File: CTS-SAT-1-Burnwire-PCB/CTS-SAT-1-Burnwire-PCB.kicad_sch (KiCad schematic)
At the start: 8 parts, among them J1 Conn_01x04_MountingPin, J2 Conn_01x06_MountingPin, Q1 IPD90N04S4L

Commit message: Layout and routing
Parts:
- added C1: 10u, Capacitor_SMD:C_1206_3216Metric_Pad1.33x1.80mm_HandSolder, symbol Device:C
- added C2: 100n, Capacitor_SMD:C_1206_3216Metric_Pad1.33x1.80mm_HandSolder, symbol Device:C
- added D2: LED, LED_SMD:LED_0603_1608Metric_Pad1.05x0.95mm_HandSolder, symbol Device:LED
- added H1, H3: MountingHole_Pad, MountingHole:MountingHole_2.2mm_M2_Pad, symbol Mechanical:MountingHole_Pad
- added H2, H4: MountingHole_Pad, MountingHole:MountingHole_2.7mm_M2.5_Pad, symbol Mechanical:MountingHole_Pad
- added R4, R5, R6, R7: 0, Resistor_SMD:R_0603_1608Metric_Pad0.98x0.95mm_HandSolder, symbol Device:R
- added R8: 5k1, Resistor_SMD:R_0603_1608Metric_Pad0.98x0.95mm_HandSolder, symbol Device:R
- added R9: 100k, Resistor_SMD:R_0603_1608Metric_Pad0.98x0.95mm_HandSolder, symbol Device:R
- J1: footprint (none) -> Connector_Molex:Molex_PicoBlade_53261-0471_1x04-1MP_P1.25mm_Horizontal
- J2: footprint (none) -> Connector_Molex:Molex_PicoBlade_53261-0671_1x06-1MP_P1.25mm_Horizontal
- R1: footprint (none) -> 00-footprint-lib:AxialBurnResistor
- R2, R3: footprint (none) -> Resistor_SMD:R_0603_1608Metric_Pad0.98x0.95mm_HandSolder
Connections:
- net BURN_CTRL: now also J1.3 (Pin_3)
- net GND: now also J1.1 (Pin_1), J1.2 (Pin_2), C1.2, C2.2, R4.2, R5.2, R6.2, R7.2, R8.2, R9.2
- net VDC: now also C1.1, C2.1
- net at D1.2 (A2), Q1.1 (G), R2.1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: now also D2.2 (A)
- net at J1.4 (Pin_4): now also R9.1
- new net: H1.1, R4.1
- new net: D2.1 (K), R8.1
- new net: H3.1, R6.1
- new net: H2.1, R5.1
- new net: H4.1, R7.1

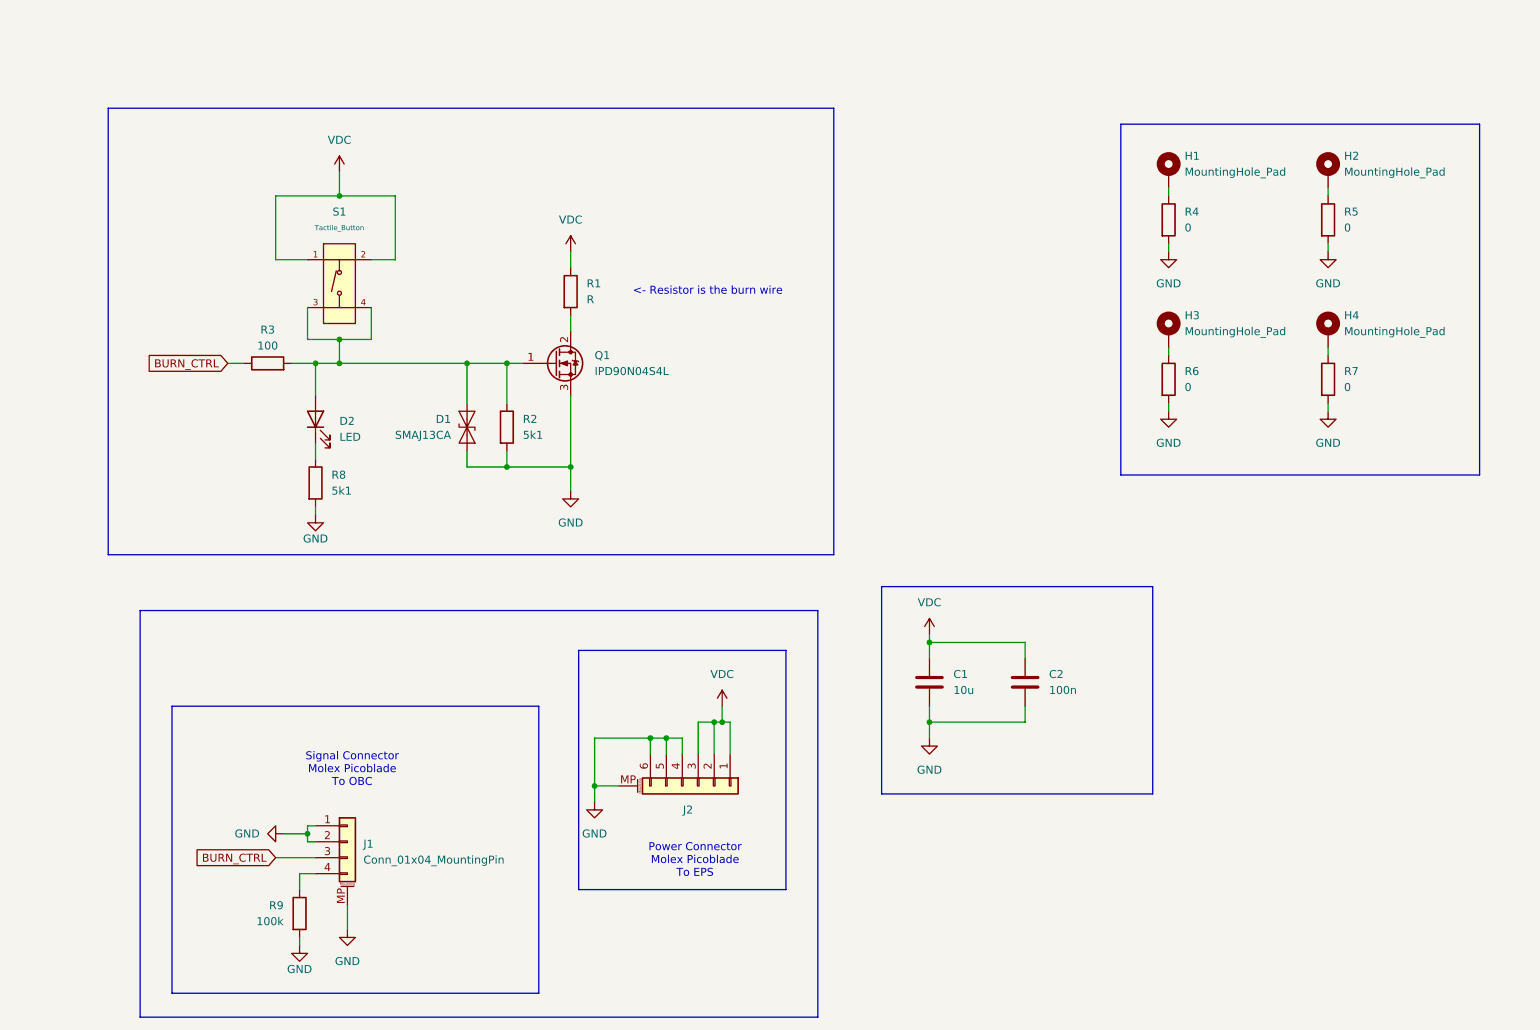
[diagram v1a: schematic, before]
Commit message: Convert to 2-resistor design
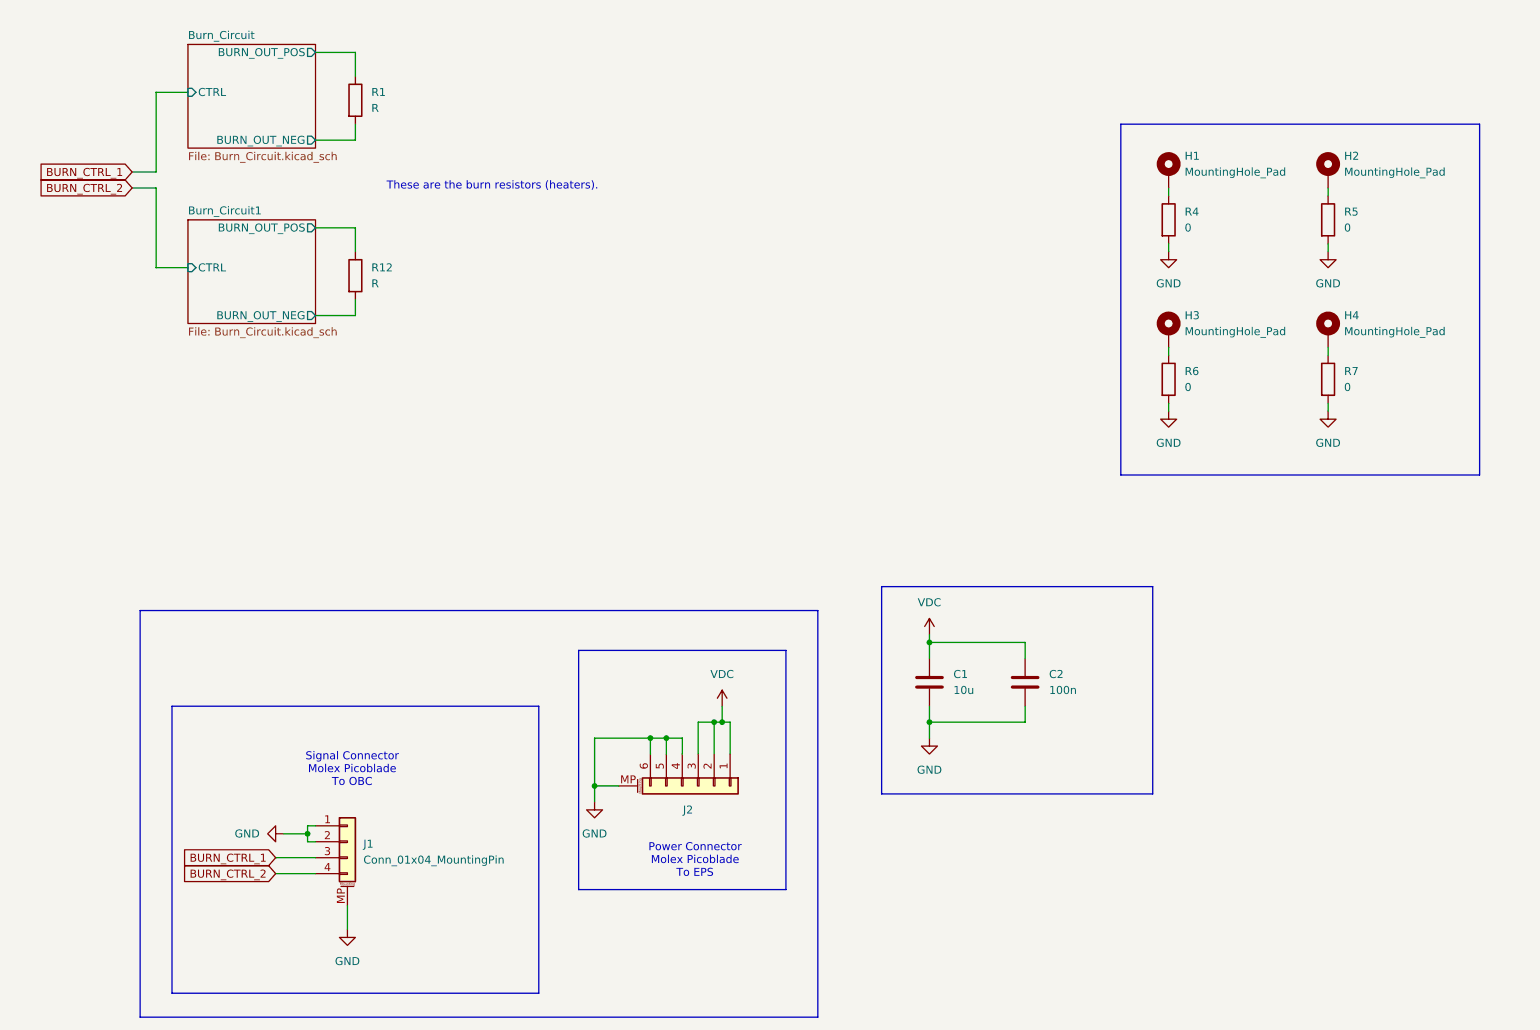
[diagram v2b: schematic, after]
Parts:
- removed D1: SMAJ13CA, Diode_SMD:D_SMA, symbol Diode:SMAJ13CA
- removed D2: LED, LED_SMD:LED_0603_1608Metric_Pad1.05x0.95mm_HandSolder, symbol Device:LED
- removed Q1: IPD90N04S4L, Package_TO_SOT_SMD:TO-252-3_TabPin2, symbol 00-symbol-lib:IPD90N04S4L
- removed R2, R8: 5k1, Resistor_SMD:R_0603_1608Metric_Pad0.98x0.95mm_HandSolder, symbol Device:R
- removed R3: 100, Resistor_SMD:R_0603_1608Metric_Pad0.98x0.95mm_HandSolder, symbol Device:R
- removed R9: 100k, Resistor_SMD:R_0603_1608Metric_Pad0.98x0.95mm_HandSolder, symbol Device:R
- removed S1: Tactile_Button, 00-footprint-lib:SW-SMD_4P-L5.1-W5.1-P3.70-LS6.5-TL-2, symbol 00-symbol-lib:Tactile_Button
- added R12: R, 00-footprint-lib:AxialBurnResistor_No_Cutout, symbol Device:R
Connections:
- net VDC: no longer R1.1
- net Burn_Circuit/BURN_OUT_NEG: now reaches R1.2
- net BURN_CTRL_2: now reaches J1.4 (Pin_4)
- net BURN_CTRL renamed BURN_CTRL_1
- new net Burn_Circuit/BURN_OUT_POS: R1.1
- new net Burn_Circuit1/BURN_OUT_NEG: R12.2
- new net Burn_Circuit1/BURN_OUT_POS: R12.1
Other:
- added sheet Burn_Circuit (Burn_Circuit.kicad_sch)
- added sheet Burn_Circuit1 (Burn_Circuit.kicad_sch)
- note added: "These are the burn resistors (heaters)."
- note removed: "<- Resistor is the burn wire"

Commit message: Update mounting hole diameters
M2 by the resistors and M2.5 by the connectors
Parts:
- H1, H3: footprint MountingHole:MountingHole_2.2mm_M2_Pad -> MountingHole:MountingHole_2.7mm_M2.5_Pad
- H2, H4: footprint MountingHole:MountingHole_2.7mm_M2.5_Pad -> MountingHole:MountingHole_2.2mm_M2_Pad
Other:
- note added: "H1 and H3 - Near connectors (M2.5)"
- note added: "H1 and H3 - Near resistors (M2)"
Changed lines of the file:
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@@
 	)
 	(rectangle
-		(start 199.39 34.29)
-		(end 256.54 90.17)
+		(start 194.31 34.29)
+		(end 264.16 90.17)
 		(stroke
 			(width 0)
@@
 		(fill
 			(type none)
+		)
+	)
+	(text "H1 and H3 - Near resistors (M2)"
+		(exclude_from_sim no)
+		(at 258.826 62.23 90)
+		(effects
+			(font
+				(size 1.27 1.27)
+			)
+		)
+	)
+	(text "H1 and H3 - Near connectors (M2.5)"
+		(exclude_from_sim no)
+		(at 198.628 62.23 90)
+		(effects
+			(font
+				(size 1.27 1.27)
+			)
 		)
 	)
@@
 			)
 		)
-		(property "Footprint" "MountingHole:MountingHole_2.2mm_M2_Pad"
+		(property "Footprint" "MountingHole:MountingHole_2.7mm_M2.5_Pad"
 			(at 207.01 41.91 0)
 			(effects
@@
 			)
 		)
-		(property "Footprint" "MountingHole:MountingHole_2.2mm_M2_Pad"
+		(property "Footprint" "MountingHole:MountingHole_2.7mm_M2.5_Pad"
 			(at 207.01 67.31 0)
 			(effects
@@
 			)
 		)
-		(property "Footprint" "MountingHole:MountingHole_2.7mm_M2.5_Pad"
+		(property "Footprint" "MountingHole:MountingHole_2.2mm_M2_Pad"
 			(at 232.41 41.91 0)
 			(effects
@@
 			)
 		)
-		(property "Footprint" "MountingHole:MountingHole_2.7mm_M2.5_Pad"
+		(property "Footprint" "MountingHole:MountingHole_2.2mm_M2_Pad"
 			(at 232.41 67.31 0)
 			(effects

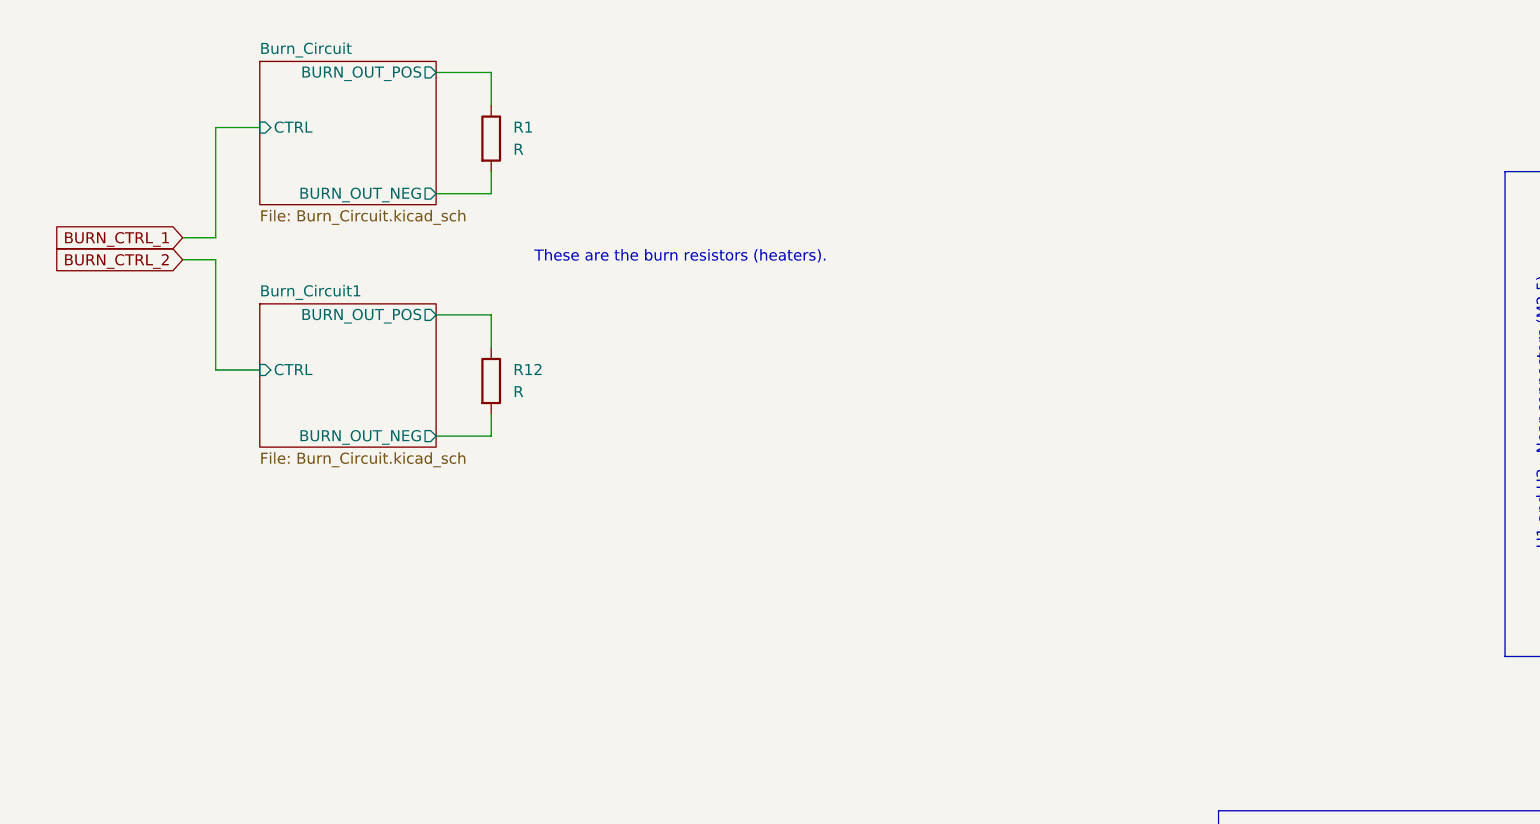
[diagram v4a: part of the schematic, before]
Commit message: Add power indicator LED
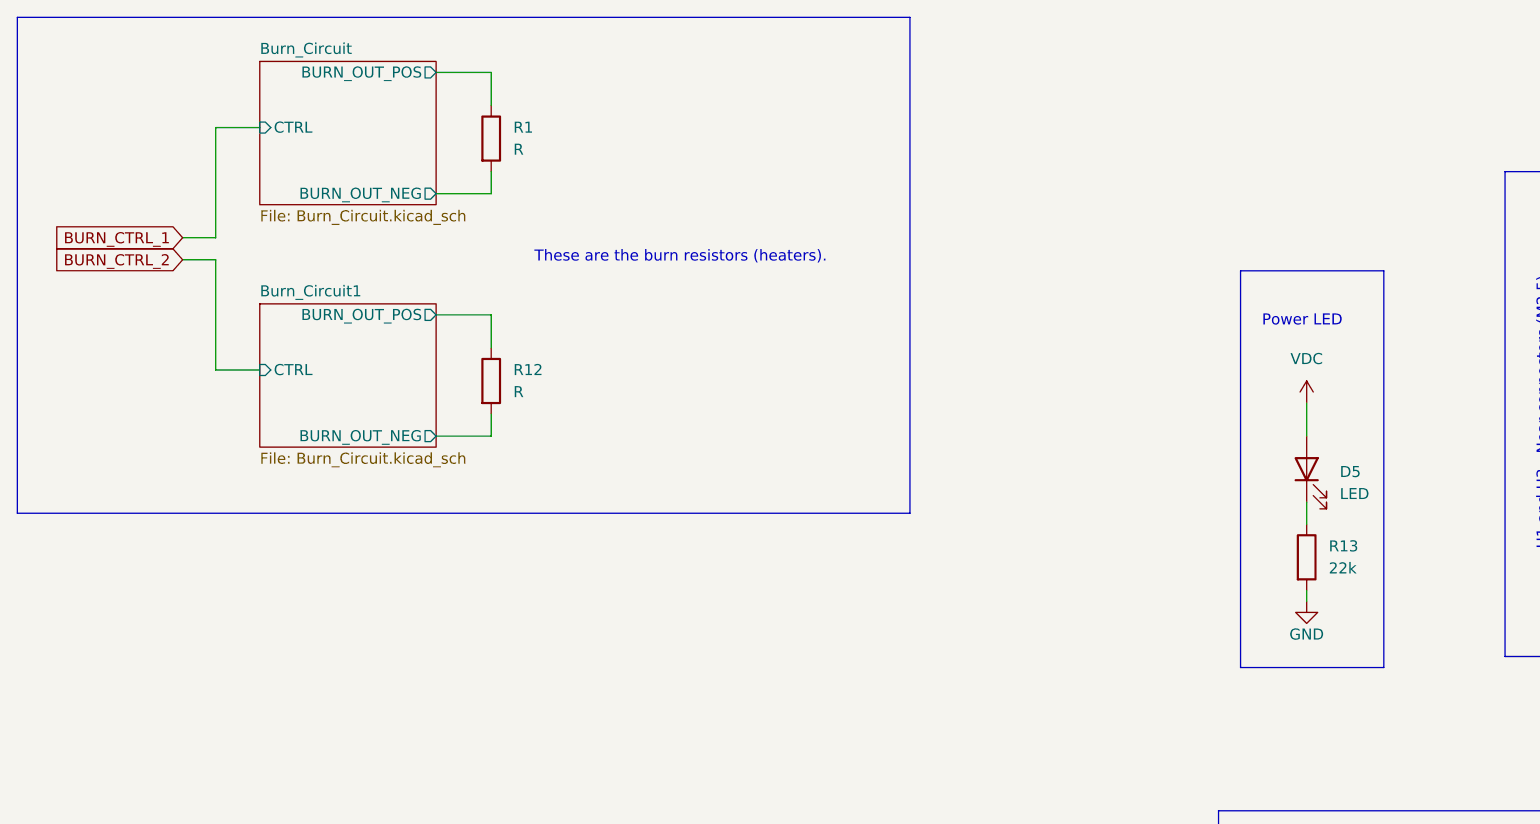
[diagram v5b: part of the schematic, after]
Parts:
- added D5: LED, LED_SMD:LED_0603_1608Metric_Pad1.05x0.95mm_HandSolder, symbol Device:LED
- added R13: 22k, Resistor_SMD:R_0603_1608Metric_Pad0.98x0.95mm_HandSolder, symbol Device:R
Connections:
- net GND: now also R13.2
- net VDC: now also D5.2 (A)
- new net: D5.1 (K), R13.1
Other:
- note added: "Power LED"

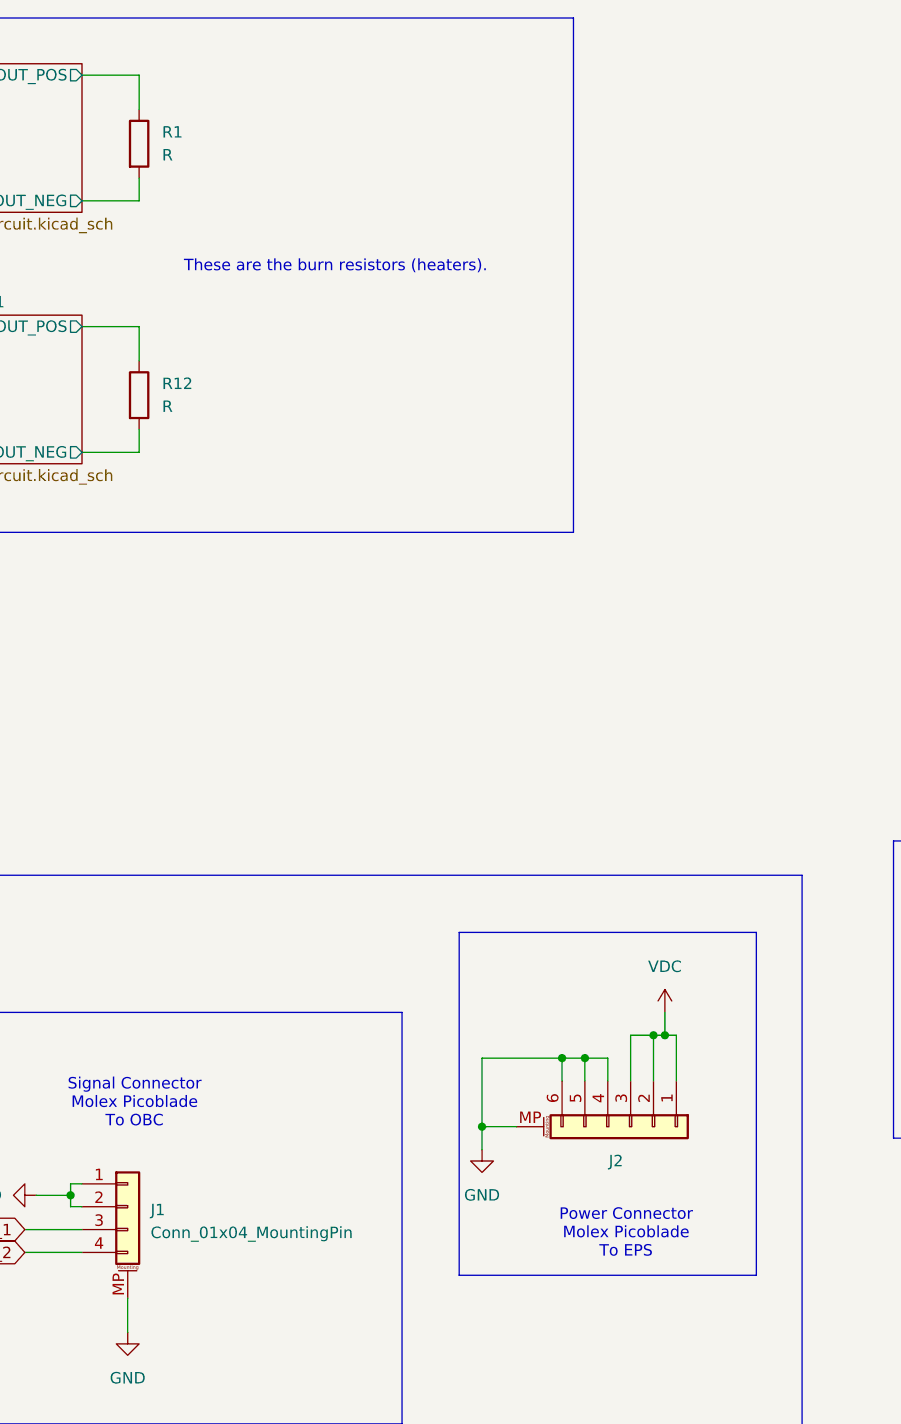
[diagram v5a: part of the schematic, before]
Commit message: Update part numbers in schematic
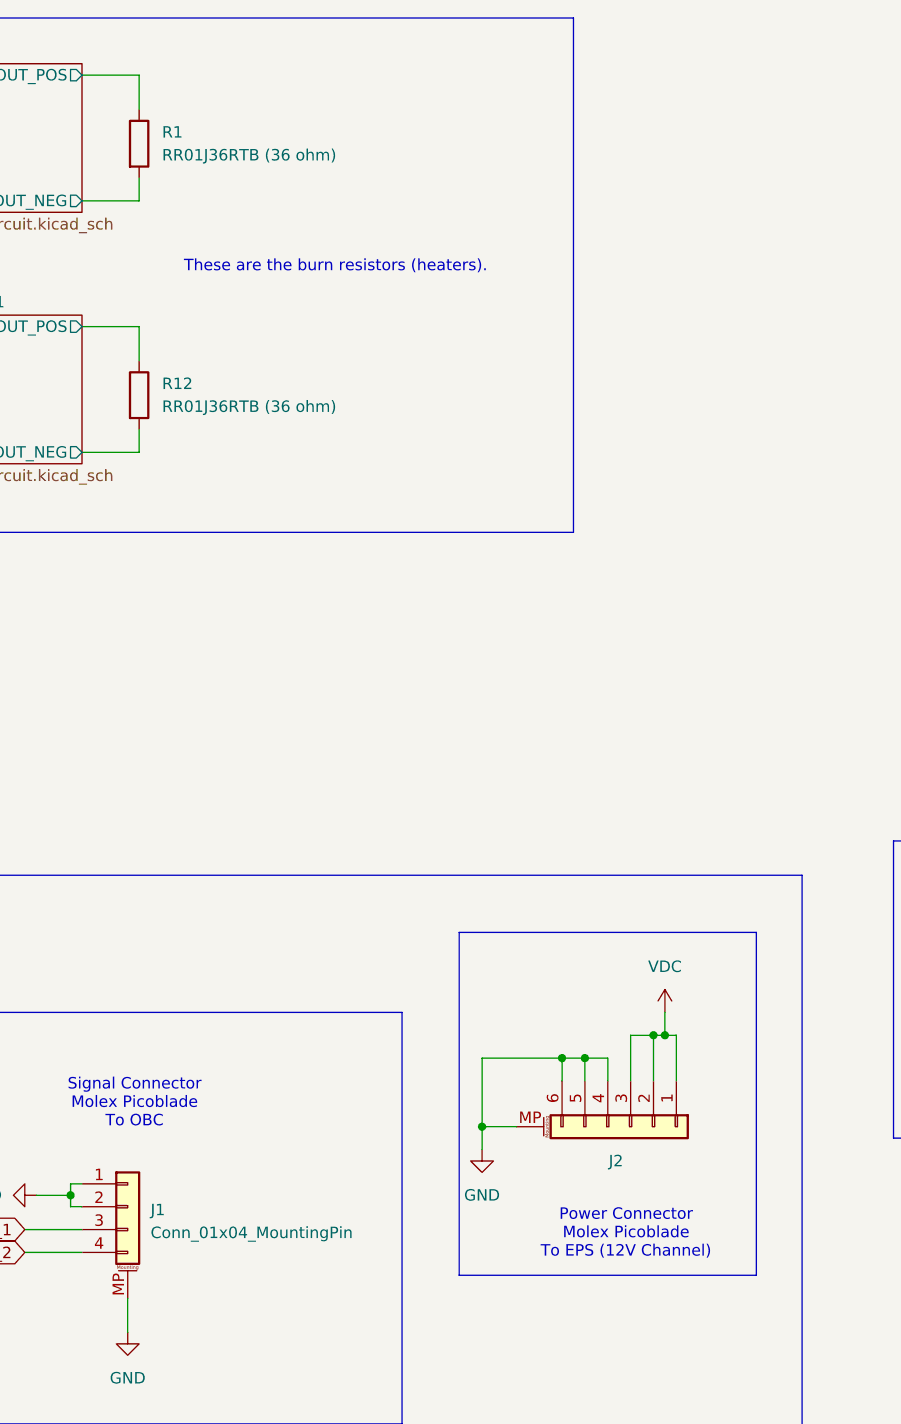
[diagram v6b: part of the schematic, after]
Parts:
- R1, R12: value R -> RR01J36RTB (36 ohm)
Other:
- note added: "Power Connector Molex Picoblade To EPS (12V Channel)"
- note removed: "Power Connector Molex Picoblade To EPS"
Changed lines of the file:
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@@
 		)
 	)
-	(text "Power Connector\nMolex Picoblade\nTo EPS"
+	(text "Power Connector\nMolex Picoblade\nTo EPS (12V Channel)"
 		(exclude_from_sim no)
 		(at 131.572 151.638 0)
@@
 			)
 		)
-		(property "Value" "R"
+		(property "Value" "RR01J36RTB (36 ohm)"
 			(at 80.01 31.7499 0)
 			(effects
@@
 		(on_board yes)
 		(dnp no)
-		(fields_autoplaced yes)
 		(property "Reference" "R12"
 			(at 80.01 57.1499 0)
@@
 			)
 		)
-		(property "Value" "R"
+		(property "Value" "RR01J36RTB (36 ohm)"
 			(at 80.01 59.6899 0)
 			(effects
